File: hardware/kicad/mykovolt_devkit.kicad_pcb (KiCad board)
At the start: 4 copper layers, 30 x 20 mm, 57 parts, among them J1 SWD_2x5, J2 Pressling, J3 Aux_I2C, J4 Sensor_In, Q1 SI1308EDL, U1 STM32L011F4Px, U2 BQ25570, U3 ST25DV04K, U4 MB85RC16, U5 PCF8523T, U6 FDC1004, X1 32.768kHz

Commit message: feat: critical path — NFC antenna, sensor electrodes, firmware startup
PCB geometry (pcbnew tracks + zones):
- NFC antenna coil: 4-turn rectangular spiral on F.Cu (18×12mm outer,
  0.3mm trace/space, ~2.9µH target for 13.56MHz with C20=47pF)
- GND keepout on In1.Cu under antenna (prevents coupling with
  copper pour, IsKeepout=True)
- Interdigital sensor electrodes on B.Cu: 10-finger comb pairs for
  CIN1 (measurement) and CIN2 (reference), SHLD1 guard ring
- Routing from electrodes through J4 to FDC1004
- 44 tracks total (17 F.Cu antenna + 27 B.Cu sensor)
- 3 zones (GND pour, antenna keepout, 3.3V pour)

Firmware startup (compilation-enabling):
- startup/startup_stm32l011xx.s — reset vector + 32 interrupt vectors
  for Cortex-M0+, BSS clear, data copy, weak default handlers
- startup/STM32L011F4Px.ld — linker script (16KB flash @ 0x08000000,
  2KB RAM @ 0x20000000, 512B stack, 256B heap)
- CMakeLists.txt — cleaned up duplicate STARTUP_SRC

Generator: 57 components, 35 nets, 185 connections, 44 tracks
Verification: 22/22 checks pass, 0 warnings, 0 errors
Tests: 85/85 pass
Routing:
- net (no net): track 0.00 -> 145.9 mm
- net SHLD1: track 0.00 -> 22.6 mm
- net CIN1: track 0.00 -> 21.3 mm
- net CIN2: track 0.00 -> 20.4 mm
- net NFC_RF1: track 0.00 -> 15.0 mm
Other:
- board text added: "NFC ANT"
- board text added: "SENSOR"

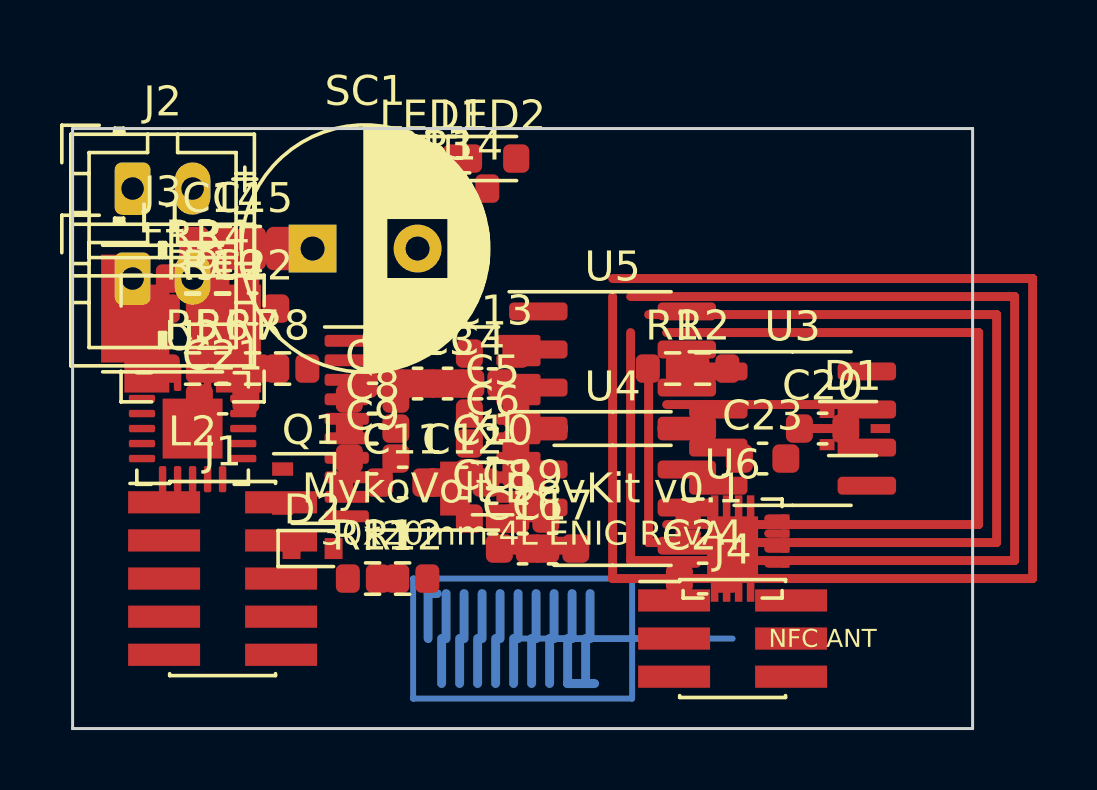
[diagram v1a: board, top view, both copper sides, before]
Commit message: feat: route I2C bus, SWD, UART, control signals + power via stitching
Routing (81 tracks + 12 vias across all layers):
- I2C bus (SCL/SDA): horizontal trunk at Y=11mm with vertical drops
  to U1→U3→U4→U5→U6 (daisy chain), 0.3mm tracks, 18 unique nets
- SWD debug (SWDIO/SWCLK/NRST): J1→U1 Manhattan routing
- UART (TX/RX): U1→J1 direct connections
- Control signals: NFC_IRQ, RTC_INT, SENSOR_RDY, VBAT_OK,
  LOAD_SW_GATE, MCU_LED_CTRL — L-shaped routes
- V_SENSE: voltage divider routing U1→R9/R10
- Power via stitching: 12 vias near ICs connecting 3.3V pads to
  In2.Cu pour and GND pads to In1.Cu pour (0.5mm via, 0.25mm drill)
- Fixed IsKeepout flag: GND/3.3V zones explicitly set to non-keepout

Generator: 57 components, 35 nets, 185 connections, 81 tracks, 12 vias
Verification: 22/22 checks pass, 0 warnings, 0 errors
Tests: 85/85 pass
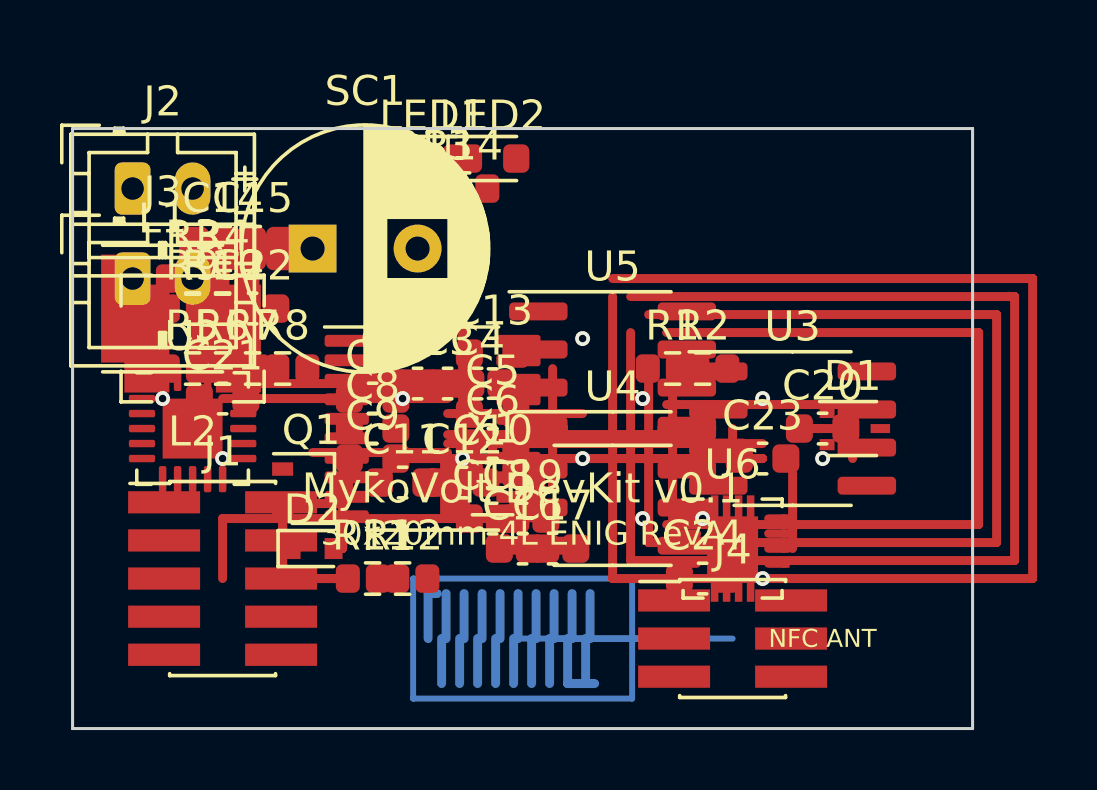
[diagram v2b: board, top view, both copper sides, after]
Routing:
- net I2C1_SDA: track 0.00 -> 20.0 mm
- net I2C1_SCL: track 0.00 -> 20.0 mm
- net NRST: track 0.00 -> 11.0 mm
- net NFC_IRQ: track 0.00 -> 10.5 mm
- net MCU_LED_CTRL: track 0.00 -> 10.0 mm
- net SENSOR_RDY: track 0.00 -> 8.50 mm
- net VBAT_OK: track 0.00 -> 7.50 mm
- net V_SENSE: track 0.00 -> 7.00 mm
- net SWDIO: track 0.00 -> 6.00 mm
- net SWCLK: track 0.00 -> 6.00 mm
- net RTC_INT: track 0.00 -> 4.50 mm
- net LOAD_SW_GATE: track 0.00 -> 4.50 mm
- net UART_TX: track 0.00 -> 2.00 mm
- net UART_RX: track 0.00 -> 2.00 mm
- net GND: vias 0 -> 6
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
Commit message: feat: complete PCB routing (35/35 nets) + Gerber export + JLCPCB files
Final routing coverage:
- BQ25570 power path: LBOOST, LBUCK, VSTOR, V_PRESSLING (0.5mm tracks)
- BQ25570 programming: OK_HYST, OK_PROG, VOC_SAMP, VOUT_SET, VRDIV, VREF_SAMP
- LEDs: LED_PWR (Q1→R13→LED1), LED_STAT (R14→LED2)
- Crystal: XTAL_IN, XTAL_OUT (U1→X1→C16/C17)
- NFC_RF2: antenna feed to C20/U3 connection
- I2C bus: fixed trunk routing (SCL/SDA both connected)
- SWD: offset routing for SWDIO/SWCLK
- UART: separated TX/RX routes
- I2C pull-ups: R1→SCL, R2→SDA vertical drops

Gerber export (12 files, via pcbnew PLOT_CONTROLLER):
- F_Cu, In1_Cu, In2_Cu, B_Cu, F_SilkS, B_SilkS
- F_Mask, B_Mask, F_Paste, B_Paste, Edge_Cuts
- NC Drill (Excellon) — JLCPCB-compatible

PCB: 108 tracks, 12 vias, 3 zones, 4-layer, 30x20mm
Nets: 35/35 covered (33 with tracks, 2 with pours)
Verification: 22/22 pass, 0 errors
Tests: 85/85 pass
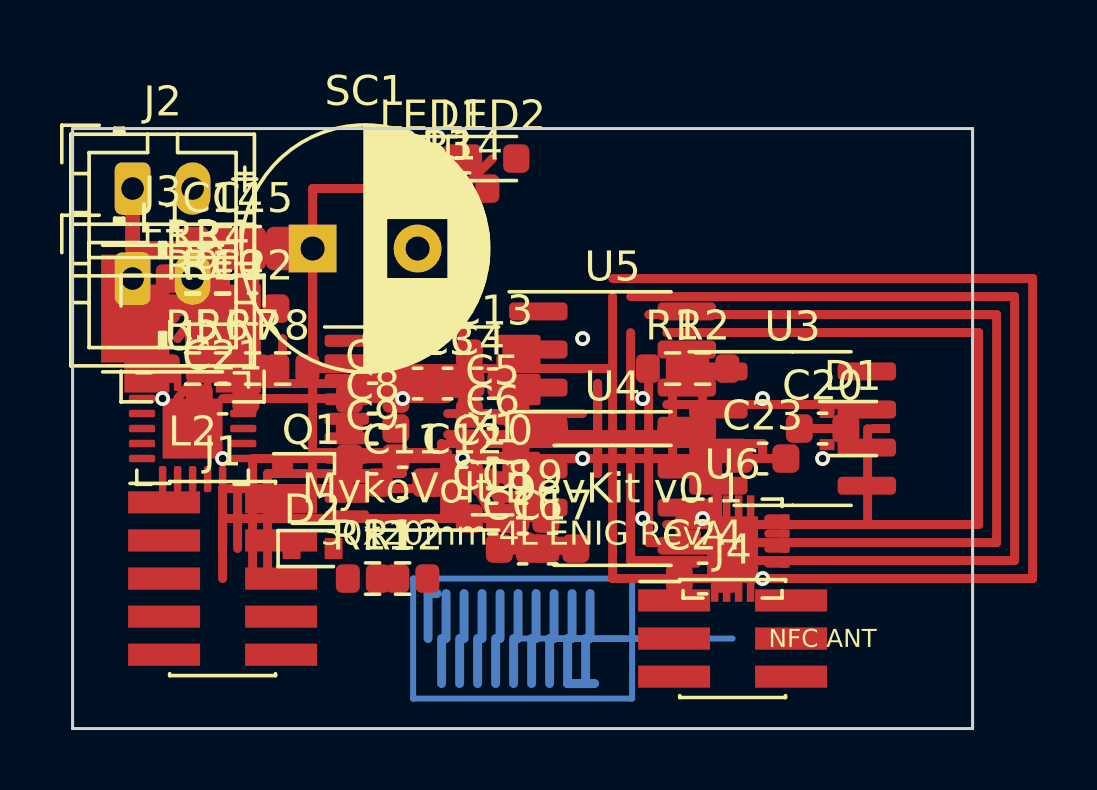
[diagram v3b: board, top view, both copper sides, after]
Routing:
- net VSTOR: track 0.00 -> 21.0 mm
- net LED_PWR: track 0.00 -> 14.0 mm
- net V_PRESSLING: track 0.00 -> 7.00 mm
- net UART_TX: track 2.00 -> 8.00 mm
- net UART_RX: track 2.00 -> 8.00 mm
- net XTAL_OUT: track 0.00 -> 4.47 mm
- net VRDIV: track 0.00 -> 3.91 mm
- net XTAL_IN: track 0.00 -> 3.65 mm
- net SWDIO: track 6.00 -> 9.00 mm
- net NFC_RF2: track 0.00 -> 3.00 mm
- net LBOOST: track 0.00 -> 3.00 mm
- net VREF_SAMP: track 0.00 -> 2.50 mm
- net VOC_SAMP: track 0.00 -> 2.24 mm
- net I2C1_SDA: track 20.0 -> 22.2 mm
- net I2C1_SCL: track 20.0 -> 22.2 mm
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
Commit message: feat: firmware drivers (FDC1004, ST25DV04K), PCB antenna fix, KiCad 9 migration
Drivers:
- Implement fdc1004.c: full driver for TI FDC1004 capacitance sensor
- Implement st25dv04k.c: full driver for ST25DV04K NFC tag (mailbox, RF)
- Extend i2c_driver: add i2c_write_reg16 / i2c_read_reg16 for 16-bit
- Add CMSIS headers + STM32L0xx device headers for build
- Fix STM32L011 MCU header include in mykovolt.h
- Fix GPIO_OTYPER/BSRR/MODER macro names for actual CMSIS headers
- Firmware builds with zero warnings (3.8KB flash, 920B RAM)

PCB (KiCad):
- Fix NFC antenna overhang: shift 37 antenna segments 2mm left
  (outer turn now at x=30, was x=32 — fits 30mm board edge)
- Fix SENSOR label position (was at y=21, past 20mm edge)
- Fix symbol references for KiCad 9: Q_PMOS_SGD → Q_PMOS,
  STM32L011F4Px → STM32L011D_3-4_Px
- Fix generate_kicad.py: antenna center 25→23mm, outer_w 14→12mm
- Fix generate_kicad.py: keepout zone matches new antenna position
- Fix generate_kicad.py: interdigital electrode bus bars now connect
  all 10 fingers (not just first/last)
- Fix generate_kicad.py: KiCad 9 API migration (VECTOR2I, SetPlotFPText)
- Re-export Gerbers with KiCad 9.0.8 (all 12 JLCPCB layers + drill)

Docs:
- Create EXIST grant application skeleton
- Create order/build checklist for PCBs and breadboard prototype

Tests: 85/85 passing
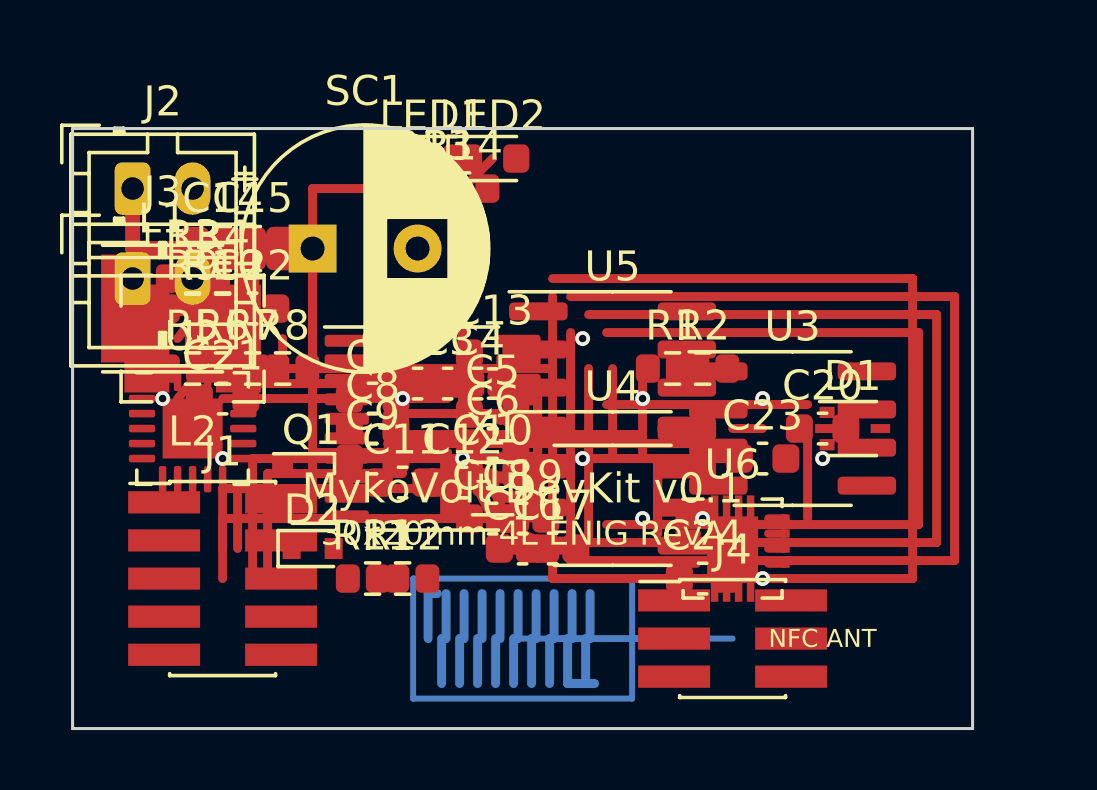
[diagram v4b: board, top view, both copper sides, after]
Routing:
- net NFC_RF1: track 15.0 -> 13.0 mm
- net (no net): track 145.9 -> 143.9 mm
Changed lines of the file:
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@@
   (gr_line (start 0 0) (end 30 0) (layer "Edge.Cuts") (width 0.1))
   (gr_line (start 30 20) (end 0 20) (layer "Edge.Cuts") (width 0.1))
-  (gr_text "SENSOR" (at 15 21) (layer "B.SilkS")
+  (gr_text "SENSOR" (at 15 16) (layer "B.SilkS")
     (effects (font (size 0.6 0.6) (thickness 0.1)))
   )
@@
     (effects (font (size 0.6 0.6) (thickness 0.1)))
   )
-  (segment (start 31.4 5.6) (end 31.4 14.4) (width 0.3) (layer "F.Cu") (net 0))
-  (segment (start 19.2 6.2) (end 30.8 6.2) (width 0.3) (layer "F.Cu") (net 0))
-  (segment (start 18 15) (end 18 5.6) (width 0.3) (layer "F.Cu") (net 0))
-  (segment (start 30.8 13.8) (end 19.2 13.8) (width 0.3) (layer "F.Cu") (net 0))
-  (segment (start 19.8 9.2) (end 26.5 9.2) (width 0.3) (layer "F.Cu") (net 0))
-  (segment (start 31.4 14.4) (end 18.6 14.4) (width 0.3) (layer "F.Cu") (net 0))
-  (segment (start 19.2 13.8) (end 19.2 8) (width 0.3) (layer "F.Cu") (net 0))
-  (segment (start 32 5) (end 32 15) (width 0.3) (layer "F.Cu") (net 0))
-  (segment (start 30.2 13.2) (end 19.8 13.2) (width 0.3) (layer "F.Cu") (net 0))
-  (segment (start 19.8 6.8) (end 30.2 6.8) (width 0.3) (layer "F.Cu") (net 0))
-  (segment (start 30.8 6.2) (end 30.8 13.8) (width 0.3) (layer "F.Cu") (net 0))
-  (segment (start 18.6 14.4) (end 18.6 6.8) (width 0.3) (layer "F.Cu") (net 0))
-  (segment (start 18.6 5.6) (end 31.4 5.6) (width 0.3) (layer "F.Cu") (net 0))
-  (segment (start 32 15) (end 18 15) (width 0.3) (layer "F.Cu") (net 0))
-  (segment (start 30.2 6.8) (end 30.2 13.2) (width 0.3) (layer "F.Cu") (net 0))
+  (segment (start 29.4 5.6) (end 29.4 14.4) (width 0.3) (layer "F.Cu") (net 0))
+  (segment (start 17.2 6.2) (end 28.8 6.2) (width 0.3) (layer "F.Cu") (net 0))
+  (segment (start 16.0 15.0) (end 16.0 5.6) (width 0.3) (layer "F.Cu") (net 0))
+  (segment (start 28.8 13.8) (end 17.2 13.8) (width 0.3) (layer "F.Cu") (net 0))
+  (segment (start 17.8 9.2) (end 24.5 9.2) (width 0.3) (layer "F.Cu") (net 0))
+  (segment (start 29.4 14.4) (end 16.6 14.4) (width 0.3) (layer "F.Cu") (net 0))
+  (segment (start 17.2 13.8) (end 17.2 8.0) (width 0.3) (layer "F.Cu") (net 0))
+  (segment (start 28.0 5.0) (end 28.0 15.0) (width 0.3) (layer "F.Cu") (net 0))
+  (segment (start 28.2 13.2) (end 17.8 13.2) (width 0.3) (layer "F.Cu") (net 0))
+  (segment (start 17.8 6.8) (end 28.2 6.8) (width 0.3) (layer "F.Cu") (net 0))
+  (segment (start 28.8 6.2) (end 28.8 13.8) (width 0.3) (layer "F.Cu") (net 0))
+  (segment (start 16.6 14.4) (end 16.6 6.8) (width 0.3) (layer "F.Cu") (net 0))
+  (segment (start 16.6 5.6) (end 29.4 5.6) (width 0.3) (layer "F.Cu") (net 0))
+  (segment (start 28.0 15.0) (end 16.0 15.0) (width 0.3) (layer "F.Cu") (net 0))
+  (segment (start 28.2 6.8) (end 28.2 13.2) (width 0.3) (layer "F.Cu") (net 0))
   (via (at 5 11) (size 0.5) (drill 0.25) (layers "F.Cu" "B.Cu") (net 1))
   (via (at 13 11) (size 0.5) (drill 0.25) (layers "F.Cu" "B.Cu") (net 1))
@@
   (via (at 17 7) (size 0.5) (drill 0.25) (layers "F.Cu" "B.Cu") (net 4))
   (via (at 23 9) (size 0.5) (drill 0.25) (layers "F.Cu" "B.Cu") (net 4))
-  (segment (start 11.3 11) (end 24 11) (width 0.3) (layer "F.Cu") (net 5))
-  (segment (start 23 10.5) (end 23 11) (width 0.3) (layer "F.Cu") (net 5))
-  (segment (start 20 8) (end 20 11) (width 0.3) (layer "F.Cu") (net 5))
+  (segment (start 9.3 11.0) (end 22.0 11.0) (width 0.3) (layer "F.Cu") (net 5))
+  (segment (start 21.0 10.5) (end 21.0 11.0) (width 0.3) (layer "F.Cu") (net 5))
+  (segment (start 18.0 8.0) (end 18.0 11.0) (width 0.3) (layer "F.Cu") (net 5))
   (segment (start 12.3 10.5) (end 12.3 11) (width 0.3) (layer "F.Cu") (net 5))
-  (segment (start 17.5 11.5) (end 17.5 11) (width 0.3) (layer "F.Cu") (net 5))
-  (segment (start 17.5 8.5) (end 17.5 11) (width 0.3) (layer "F.Cu") (net 5))
-  (segment (start 21.5 13.5) (end 21.5 11) (width 0.3) (layer "F.Cu") (net 5))
-  (segment (start 17.5 11.5) (end 17.5 11) (width 0.3) (layer "F.Cu") (net 6))
-  (segment (start 17.5 8.5) (end 17.5 11) (width 0.3) (layer "F.Cu") (net 6))
-  (segment (start 11.3 11) (end 24 11) (width 0.3) (layer "F.Cu") (net 6))
+  (segment (start 15.5 11.5) (end 15.5 11.0) (width 0.3) (layer "F.Cu") (net 5))
+  (segment (start 15.5 8.5) (end 15.5 11.0) (width 0.3) (layer "F.Cu") (net 5))
+  (segment (start 19.5 13.5) (end 19.5 11.0) (width 0.3) (layer "F.Cu") (net 5))
+  (segment (start 15.5 11.5) (end 15.5 11.0) (width 0.3) (layer "F.Cu") (net 6))
+  (segment (start 15.5 8.5) (end 15.5 11.0) (width 0.3) (layer "F.Cu") (net 6))
+  (segment (start 9.3 11.0) (end 22.0 11.0) (width 0.3) (layer "F.Cu") (net 6))
   (segment (start 12.3 10.5) (end 12.3 11) (width 0.3) (layer "F.Cu") (net 6))
-  (segment (start 23 10.5) (end 23 11) (width 0.3) (layer "F.Cu") (net 6))
-  (segment (start 21 8) (end 21 11) (width 0.3) (layer "F.Cu") (net 6))
-  (segment (start 21.5 13.5) (end 21.5 11) (width 0.3) (layer "F.Cu") (net 6))
+  (segment (start 21.0 10.5) (end 21.0 11.0) (width 0.3) (layer "F.Cu") (net 6))
+  (segment (start 19.0 8.0) (end 19.0 11.0) (width 0.3) (layer "F.Cu") (net 6))
+  (segment (start 19.5 13.5) (end 19.5 11.0) (width 0.3) (layer "F.Cu") (net 6))
   (segment (start 4 6) (end 3 6) (width 0.5) (layer "F.Cu") (net 7))
   (segment (start 4 8) (end 4 6) (width 0.5) (layer "F.Cu") (net 7))
@@
   (segment (start 12.5 11.5) (end 13 11.5) (width 0.3) (layer "F.Cu") (net 12))
   (segment (start 13 11.5) (end 13 2) (width 0.3) (layer "F.Cu") (net 12))
-  (segment (start 12.5 10.5) (end 23 10.5) (width 0.3) (layer "F.Cu") (net 13))
-  (segment (start 23 10.5) (end 23 10.5) (width 0.3) (layer "F.Cu") (net 13))
-  (segment (start 24 10) (end 25 10) (width 0.3) (layer "F.Cu") (net 14))
-  (segment (start 18 5) (end 32 5) (width 0.3) (layer "F.Cu") (net 14))
-  (segment (start 26.5 10) (end 26.5 13) (width 0.3) (layer "F.Cu") (net 15))
+  (segment (start 10.5 10.5) (end 21.0 10.5) (width 0.3) (layer "F.Cu") (net 13))
+  (segment (start 21.0 10.5) (end 21.0 10.5) (width 0.3) (layer "F.Cu") (net 13))
+  (segment (start 22.0 10.0) (end 23.0 10.0) (width 0.3) (layer "F.Cu") (net 14))
+  (segment (start 16.0 5.0) (end 28.0 5.0) (width 0.3) (layer "F.Cu") (net 14))
+  (segment (start 24.5 10.0) (end 24.5 13.0) (width 0.3) (layer "F.Cu") (net 15))
   (segment (start 5 15) (end 5 13) (width 0.3) (layer "F.Cu") (net 16))
   (segment (start 5 13) (end 14 13) (width 0.3) (layer "F.Cu") (net 16))
   (segment (start 3.5 8) (end 5 8) (width 0.3) (layer "F.Cu") (net 17))
   (segment (start 3 8) (end 4 8) (width 0.3) (layer "F.Cu") (net 18))
-  (segment (start 12.5 9.5) (end 17 9.5) (width 0.3) (layer "F.Cu") (net 19))
-  (segment (start 17 9.5) (end 17 9.5) (width 0.3) (layer "F.Cu") (net 19))
-  (segment (start 21 10.2) (end 21 10.2) (width 0.3) (layer "F.Cu") (net 20))
-  (segment (start 12.5 10.2) (end 21 10.2) (width 0.3) (layer "F.Cu") (net 20))
+  (segment (start 10.5 9.5) (end 15.0 9.5) (width 0.3) (layer "F.Cu") (net 19))
+  (segment (start 15.0 9.5) (end 15.0 9.5) (width 0.3) (layer "F.Cu") (net 19))
+  (segment (start 19.0 10.2) (end 19.0 10.2) (width 0.3) (layer "F.Cu") (net 20))
+  (segment (start 10.5 10.2) (end 19.0 10.2) (width 0.3) (layer "F.Cu") (net 20))
   (segment (start 11.35 15) (end 18.65 15) (width 0.2) (layer "B.Cu") (net 21))
   (segment (start 11.35 19) (end 11.35 15) (width 0.2) (layer "B.Cu") (net 21))
@@
   (segment (start 3.5 9) (end 6 6) (width 0.3) (layer "F.Cu") (net 29))
   (segment (start 3.5 7) (end 5 5) (width 0.3) (layer "F.Cu") (net 30))
-  (segment (start 8 8) (end 18 8) (width 0.3) (layer "F.Cu") (net 31))
+  (segment (start 6.0 8.0) (end 16.0 8.0) (width 0.3) (layer "F.Cu") (net 31))
   (segment (start 5 8) (end 5 4) (width 0.5) (layer "F.Cu") (net 31))
   (segment (start 5 4) (end 8 4) (width 0.5) (layer "F.Cu") (net 31))
